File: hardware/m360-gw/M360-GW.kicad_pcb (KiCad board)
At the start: 2 copper layers, 0 parts

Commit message: feat(hardware): posicionamento da M360-GW e LEDs fora da placa (J3)
Placa de 80 × 60 mm, 17 footprints (12 peças, 4 furos M3 e o conector), DRC 0 violações.

Duas restrições comandaram o arranjo, e nenhuma das duas aparece no DRC:

- o mezanino M360-RF ocupa 34,2 × 23 mm **acima** do soquete, mas o courtyard do soquete tem só
  6,2 × 13,8 — confiar nele teria colocado peças embaixo do módulo. J1 fica em x = borda − 27,2
  para o SMA sair pela lateral, e conferi por número que a faixa x 145,8-180 / y 100-123 está
  vazia;
- o D1 mini traz keep-out sobre a antena, na mesma ponta onde fica o USB. Essa ponta encosta na
  borda de cima: a antena não irradia para dentro do cobre e o cabo entra sem abrir a caixa.

Pelo mesmo motivo o H2 não fica no canto — ali cairia sob o mezanino, e a placa teria de ser
parafusada antes de encaixar o módulo. Mesma armadilha já evitada na ACT.

Os LEDs saíram da placa: ficam no painel da caixa e o J3 (JST XH) leva os três pares ao chicote.
São **6 vias em pares ânodo/cátodo**, e não 4 com terra comum, porque o verde é ativo em LOW — o
cátodo dele vai ao D4, não ao GND, de modo que não existe terra comum aos três. Com pares
dedicados os três são ligados da mesma forma no chicote apesar dessa assimetria, e o XH é
chaveado, o que impede inversão no campo. Os resistores de 1 kΩ ficam a bordo: limitação de
corrente não deve viajar no cabo.

O primeiro DRC acusou 5 violações, quatro delas com uma causa só: **girado 90°, o resistor não
fica centrado na origem** — o courtyard vai de y − 11,25 a y + 1,10, quase todo acima do ponto
informado. A fileira subia até 131,75 e entrava no U1, que termina em 134,79. O cálculo ficou
registrado como comentário no place_gw.py, porque se repete na próxima placa. A quinta violação
era o texto de referência do H1 cortado pela borda; como os furos são board-only e ficam fora da
BOM e do arquivo de posição, a serigrafia deles passou a invisível.

Verificação: a troca dos LEDs pelo conector alterou a netlist exatam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
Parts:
- added C1: 10u, Capacitor_THT:CP_Radial_D5.0mm_P2.00mm, F.Cu at (106.0, 140.0)
- added C2: 100n, Capacitor_THT:C_Disc_D5.0mm_W2.5mm_P5.00mm, F.Cu at (115.0, 140.0)
- added C3: 100n, Capacitor_THT:C_Disc_D5.0mm_W2.5mm_P5.00mm, F.Cu at (140.0, 130.0)
- added C4: 100n, Capacitor_THT:C_Disc_D5.0mm_W2.5mm_P5.00mm, F.Cu at (172.0, 140.0)
- added H1: MountingHole_3.2mm_M3, MountingHole_3.2mm_M3, F.Cu at (104.0, 104.0)
- added H2: MountingHole_3.2mm_M3, MountingHole_3.2mm_M3, F.Cu at (176.0, 130.0)
- added H3: MountingHole_3.2mm_M3, MountingHole_3.2mm_M3, F.Cu at (104.0, 156.0)
- added H4: MountingHole_3.2mm_M3, MountingHole_3.2mm_M3, F.Cu at (176.0, 156.0)
- added J1: Mezanino M360-RF, M360:M360-RF_Soquete_2x05, F.Cu at (152.8, 106.4)
- added J2: 5 V ext, M360:TerminalBlock_WJ500V-5.08-2P, F.Cu at (114.0, 152.0)
- added J3: LEDs (painel), Connector_JST:JST_XH_B6B-XH-A_1x06_P2.50mm_Vertical, F.Cu at (130.0, 154.0)
- added R1: 1k, Resistor_THT:R_Axial_DIN0207_L6.3mm_D2.5mm_P10.16mm_Horizontal, F.Cu at (128.0, 148.0)
- added R2: 1k, Resistor_THT:R_Axial_DIN0207_L6.3mm_D2.5mm_P10.16mm_Horizontal, F.Cu at (136.0, 148.0)
- added R3: 1k, Resistor_THT:R_Axial_DIN0207_L6.3mm_D2.5mm_P10.16mm_Horizontal, F.Cu at (144.0, 148.0)
- added R4: 10k, Resistor_THT:R_Axial_DIN0207_L6.3mm_D2.5mm_P10.16mm_Horizontal, F.Cu at (165.0, 140.0)
- added SW1: AP / reset, Button_Switch_THT:SW_PUSH_6mm, F.Cu at (152.0, 152.0)
- added U1: WEMOS D1 mini, RF_Module:WEMOS_D1_mini_light, F.Cu at (110.0, 108.5)
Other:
- board outline added: 80 x 60 mm

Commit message: feat(hardware): roteamento, planos de terra e serigrafia da M360-GW
Roteamento pelo Freerouting 1.9.0 na linha de comando (§11): 0,69 s de roteamento e 4,01 s de
otimização, ~52,77% de melhoria. Resultado: **133 segmentos e 1 via**, zero ligações pendentes
(eram 33). Uma via só não é erro: numa placa 100% THT cada ilha já atravessa as duas faces, e o
roteador troca de camada nos próprios furos.

Planos de GND nas duas faces, isolamento de 0,25 mm, cada um com um polígono contíguo.

O preenchimento acusou `starved_thermal` na ilha 2 do J3 — a ilha de terra do conector dos LEDs,
com 1 raio conectado onde o DRC exige 2. Foi o mesmo sintoma dos RJ45 na LP e na ACT, mas aqui
**o passo 1 da §11.4 bastou**: hastes de 0,35 mm com folga de 0,3 resolveram, sem precisar da
ligação sólida. A geometria explica: as ilhas do JST XH são 1,7 × 1,95 mm a passo de 2,5, o que
deixa só 0,3 mm de corredor horizontal entre ilhas vizinhas — mas os raios verticais passam a
caber assim que a folga cai de 0,5 para 0,3.

Duas armadilhas encontradas e registradas:

- **`set_design_rules` não persiste a largura de trilha que informa.** A ferramenta respondeu
  `trackWidth: 0.25`, mas gravou 0,2 na netclass "Default" do `.kicad_pro` — o valor mínimo — e
  o DSN saiu com `(width 200)`. Quem o roteador lê é o DSN. Corrigido direto no `.kicad_pro` e
  reexportado, agora com `(width 250)`. O aviso está na §11.2. O `kicad-cli` não exporta DSN
  (a lista de subcomandos não tem Specctra), então o MCP é o único caminho automatizado.
- **"Auto-save refused" nem sempre quer dizer o mesmo.** Nas sincronizações o aviso foi
  pessimista duas vezes e a gravação tinha ocorrido; no `add_copper_pour` foi legítimo e a zona
  só existia em memória — conferido no arquivo, onde a única zona era o keep-out do D1 mini.
  Recuperado pelo caminho documentado: recarregar e reaplicar, nunca forçar a gravação.

Serigrafia: marca "Viridiotech.com.br" na faixa livre entre o mezanino e o C3/R4. A primeira
posição encostava na 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
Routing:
- net GND: track 0.00 -> 147.6 mm
- net +3V3: track 0.00 -> 110.9 mm, vias 0 -> 1
- net A0_BTN: track 0.00 -> 108.9 mm
- net LED_YELLOW: track 0.00 -> 57.9 mm
- net MISO: track 0.00 -> 48.7 mm
- net MOSI: track 0.00 -> 48.5 mm
- net NSS: track 0.00 -> 47.5 mm
- net SCK: track 0.00 -> 45.4 mm
- net +5V: track 0.00 -> 41.9 mm
- net LED_GREEN_K: track 0.00 -> 37.5 mm
- net LED_RED: track 0.00 -> 34.1 mm
- net LED_GREEN_A: track 0.00 -> 19.4 mm
- net DIO0: track 0.00 -> 19.3 mm
- net LED_RED_A: track 0.00 -> 18.3 mm
- net LED_YELLOW_A: track 0.00 -> 17.5 mm
- added copper zone on B.Cu, net GND
- added copper zone on F.Cu, net GND
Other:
- board text added: "Viridiotech.com.br"

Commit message: fix(hardware): GW — borne J2 com a entrada dos fios para a borda esquerda
J2 (C8465) a rot 90 em (106; 147): a entrada do fio é o lado -y do footprint
(datasheet, corte A-A) e em rot 0 olhava para dentro da placa. C1 sobe 2 mm.
A placa da GW segue defasada (versão THT) até ser refeita em SMD.

Co-Authored-By: Claude Opus 5 (1M context) <noreply@anthropic.com>
Claude-Session: https://claude.ai/code/session_012t7RkcrXvvpDVjKVimNu18
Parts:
- moved J2 9.43 mm to (106.0, 147.0), turned to 90 degrees
- moved C1 2.00 mm to (106.0, 138.0)
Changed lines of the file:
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@@
 	(footprint "Capacitor_THT:CP_Radial_D5.0mm_P2.00mm"
 		(layer "F.Cu")
-		(at 106 140)
+		(at 106 138)
 		(descr "CP, Radial series, Radial, pin pitch=2.00mm, diameter=5mm, height=7mm, Electrolytic Capacitor")
 		(tags "CP Radial series Radial pin pitch 2.00mm diameter 5mm height 7mm Electrolytic Capacitor")
@@
 	(footprint "M360:TerminalBlock_WJ500V-5.08-2P"
 		(layer "F.Cu")
-		(at 114 152)
+		(at 106 147 90)
 		(descr "WJ500V-5.08-2P")
 		(property "Reference" "J2"
-			(at 0 -4 0)
+			(at 0 -4 90)
 			(layer "F.SilkS")
 			(effects
@@
 		)
 		(property "Value" "5 V ext"
-			(at 0 4 0)
+			(at 0 4 90)
 			(layer "F.Fab")
 			(effects
@@
 		)
 		(property "Datasheet" ""
-			(at 0 0 0)
+			(at 0 0 90)
 			(layer "F.Fab")
 			(hide yes)
@@
 		)
 		(property "Description" ""
-			(at 0 0 0)
+			(at 0 0 90)
 			(layer "F.Fab")
 			(hide yes)
@@
 		)
 		(property "LCSC Part" "C8465"
-			(at 0 0 0)
+			(at 0 0 90)
 			(layer "F.Fab")
 			(hide yes)
@@
 		(duplicate_pad_numbers_are_jumpers no)
 		(fp_line
+			(start 5.08 -5.64)
+			(end -5.05 -5.64)
+			(stroke
+				(width 0.25)
+				(type solid)
+			)
+			(layer "F.SilkS")
+		)
+		(fp_line
 			(start -5.68 -4.75)
 			(end -5.68 -3.75)
@@
 		)
 		(fp_line
+			(start -5.08 -4.5)
+			(end -5.68 -4.75)
+			(stroke
+				(width 0.25)
+				(type solid)
+			)
+			(layer "F.SilkS")
+		)
+		(fp_line
 			(start -5.68 -3.75)
 			(end -5.08 -4)
@@
 		)
 		(fp_line
+			(start -5.08 3)
+			(end -5.68 2.75)
+			(stroke
+				(width 0.25)
+				(type solid)
+			)
+			(layer "F.SilkS")
+		)
+		(fp_line
 			(start -5.68 3.75)
 			(end -5.08 3.5)
@@
 		)
 		(fp_line
-			(start -5.08 -4.5)
-			(end -5.68 -4.75)
+			(start 5.08 4.52)
+			(end 5.08 -5.64)
 			(stroke
 				(width 0.25)
@@
 		)
 		(fp_line
-			(start -5.08 3)
-			(end -5.68 2.75)
+			(start 5.08 4.52)
+			(end -5.05 4.52)
 			(stroke
 				(width 0.25)
@@
 			(start -5.08 4.52)
 			(end -5.08 -5.64)
-			(stroke
-				(width 0.25)
-				(type solid)
-			)
-			(layer "F.SilkS")
-		)
-		(fp_line
-			(start 5.08 -5.64)
-			(end -5.05 -5.64)
-			(stroke
-				(width 0.25)
-				(type solid)
-			)
-			(layer "F.SilkS")
-		)
-		(fp_line
-			(start 5.08 4.52)
-			(end -5.05 4.52)
-			(stroke
-				(width 0.25)
-				(type solid)
-			)
-			(layer "F.SilkS")
-		)
-		(fp_line
-			(start 5.08 4.52)
-			(end 5.08 -5.64)
 			(stroke
 				(width 0.25)
@@
 			)
 			(fill no)
+			(layer "F.SilkS")
+		)
+		(fp_poly
+			(pts
+				(xy 2.080006 -5.499989) (xy 3.080004 -5.499989) (xy 3.080004 -3.499993) (xy 3.580003 -3.499993)
+				(xy 2.580005 -2.499995) (xy 1.580007 -3.499993) (xy 2.080006 -3.499993) (xy 2.080006 -5.499989)
+			)
+			(stroke
+				(width 0)
+				(type solid)
+			)
+			(fill yes)
 			(layer "F.SilkS")
 		)
@@
 			(layer "F.SilkS")
 		)
-		(fp_poly
-			(pts
-				(xy 2.080006 -5.499989) (xy 3.080004 -5.499989) (xy 3.080004 -3.499993) (xy 3.580003 -3.499993)
-				(xy 2.580005 -2.499995) (xy 1.580007 -3.499993) (xy 2.080006 -3.499993) (xy 2.080006 -5.499989)
-			)
-			(stroke
-				(width 0)
-				(type solid)
-			)
-			(fill yes)
-			(layer "F.SilkS")
+		(fp_line
+			(start 5.21 -5.5)
+			(end 5.21 4.5)
+			(stroke
+				(width 0.05)
+				(type solid)
+			)
+			(layer "F.CrtYd")
 		)
 		(fp_line
@@
 		)
 		(fp_line
+			(start 5.21 4.5)
+			(end -5.21 4.5)
+			(stroke
+				(width 0.05)
+				(type solid)
+			)
+			(layer "F.CrtYd")
+		)
+		(fp_line
 			(start -5.21 4.5)
 			(end -5.21 -5.5)
@@
 			(layer "F.CrtYd")
 		)
-		(fp_line
-			(start 5.21 -5.5)
-			(end 5.21 4.5)
-			(stroke
-				(width 0.05)
-				(type solid)
-			)
-			(layer "F.CrtYd")
-		)
-		(fp_line
-			(start 5.21 4.5)
-			(end -5.21 4.5)
-			(stroke
-				(width 0.05)
-				(type solid)
-			)
-			(layer "F.CrtYd")
+		(fp_circle
+			(center 2.54 0)
+			(end 2.82 0)
+			(stroke
+				(width 0.55)
+				(type solid)
+			)
+			(fill no)
+			(layer "F.Fab")
 		)
 		(fp_circle
@@
 			(layer "F.Fab")
 		)
-		(fp_circle
-			(center 2.54 0)
-			(end 2.82 0)
-			(stroke
-				(width 0.55)
-				(type solid)
-			)
-			(fill no)
-			(layer "F.Fab")
-		)
 		(fp_text user "${REFERENCE}"
-			(at 0 0 0)
+			(at 0 0 90)
 			(layer "F.Fab")
 			(effects
@@
 		)
 		(pad "1" thru_hole circle
-			(at -2.54 0 180)
+			(at -2.54 0 270)
 			(size 2 2)
 			(drill 1.300022)
@@
 		)
 		(pad "2" thru_hole circle
-			(at 2.54 0 180)
+			(at 2.54 0 270)
 			(size 2 2)
 			(drill 1.300022)

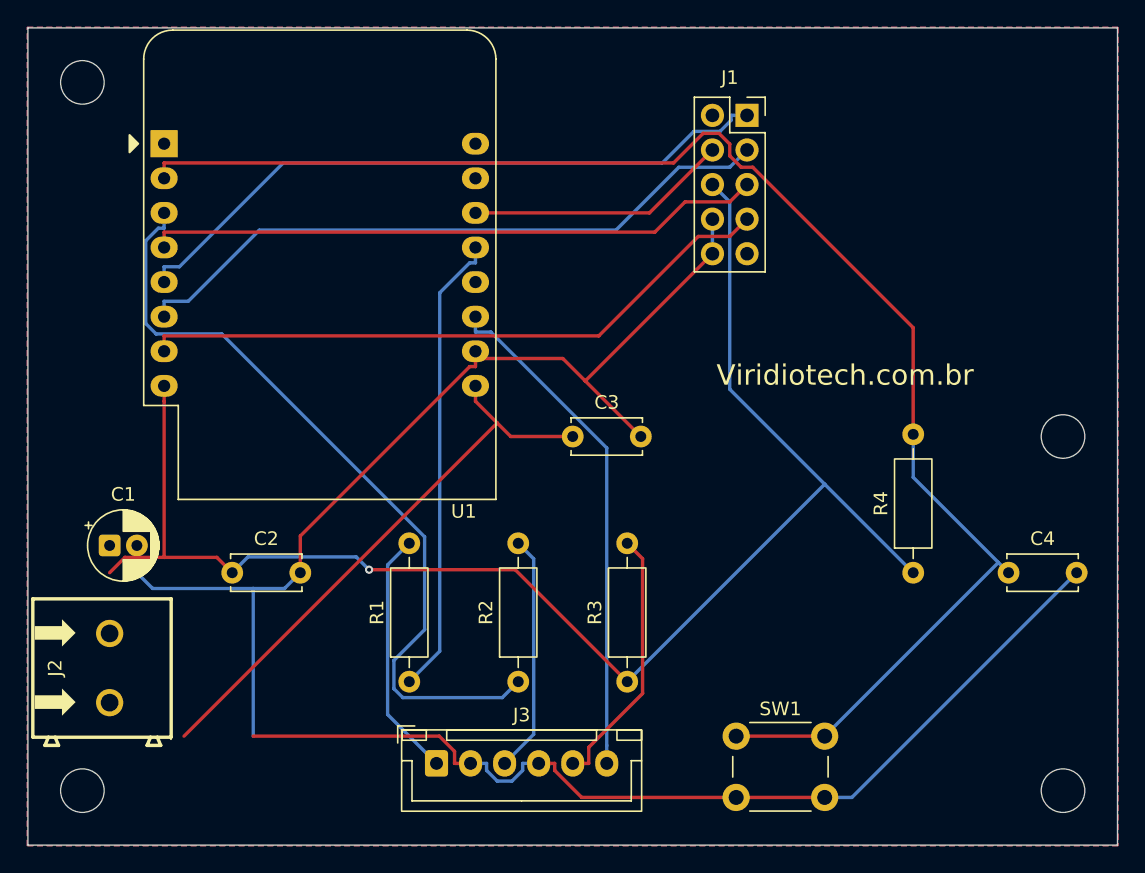
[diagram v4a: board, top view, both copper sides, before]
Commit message: feat(hardware): placa da M360-GW refeita em SMD e arquivos de fabricação
- 10 footprints THT apagados, 15 SMD sincronizados do esquemático
- place_gw.py reescrito: D1 mini com a antena na borda de cima, mezanino com
  o SMA na borda direita, borne J2 a rot 90 (entrada dos fios na borda),
  reed a 1 mm da borda esquerda junto do A0, cadeia SS14 -> PTC -> SMAJ,
  resistores dos LEDs e 2N7002 junto do J3, fiduciais
- classe Power em VIN_RAW, VIN_POL, +5V e +3V3
- vias_gnd.py: isolamento da classe do pad e áreas proibidas de footprint
  (keep-out da antena do D1 mini)
- fabricacao/: 14 peças, todas com LCSC

DRC --severity-all 0/0, paridade idêntica.

Co-Authored-By: Claude Opus 5 (1M context) <noreply@anthropic.com>
Claude-Session: https://claude.ai/code/session_012t7RkcrXvvpDVjKVimNu18
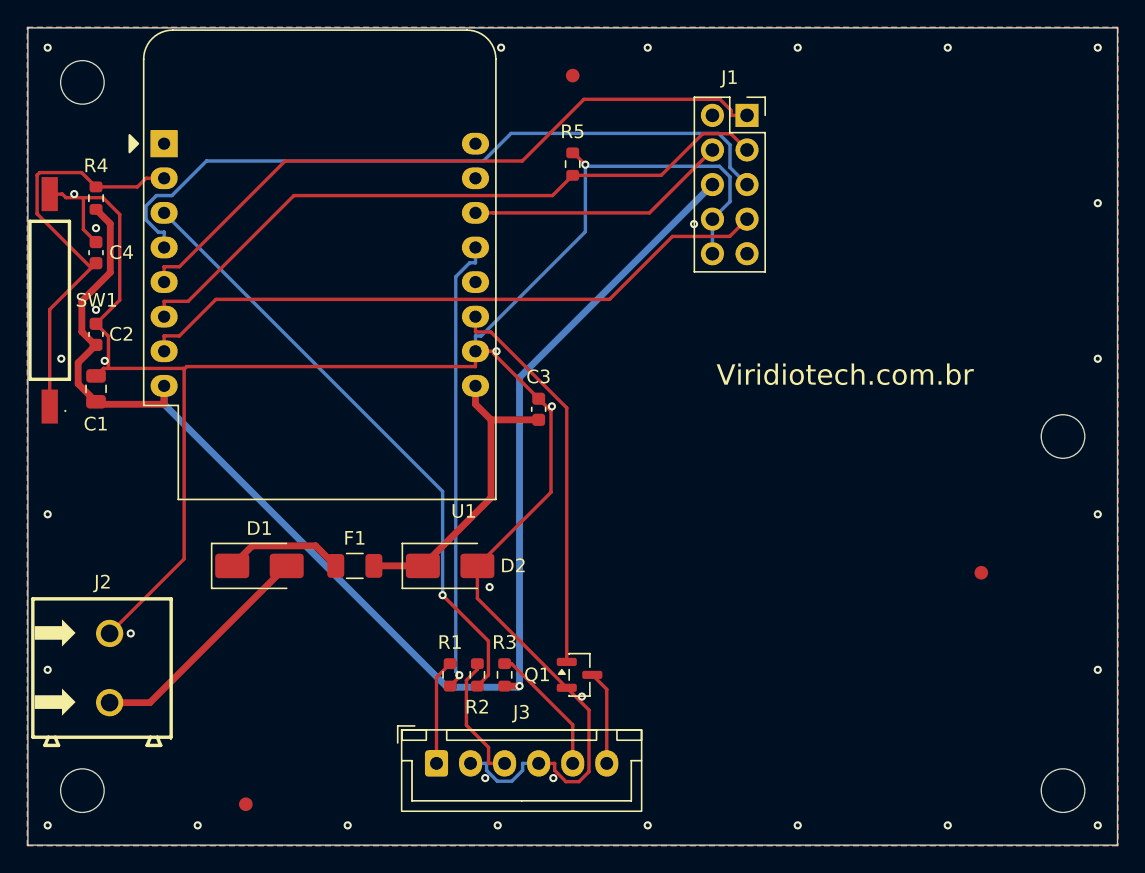
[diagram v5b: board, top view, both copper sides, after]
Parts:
- added D1: SS14, Diode_SMD:D_SMA, F.Cu at (117.0, 139.5)
- added D2: SMAJ5.0A, Diode_SMD:D_SMA, F.Cu at (131.0, 139.5)
- added F1: 500mA, Fuse:Fuse_1206_3216Metric, F.Cu at (124.0, 139.5)
- added FID1: Fiducial_1mm_Mask2mm, Fiducial_1mm_Mask2mm, F.Cu at (140.0, 103.5)
- added FID2: Fiducial_1mm_Mask2mm, Fiducial_1mm_Mask2mm, F.Cu at (170.0, 140.0)
- added FID3: Fiducial_1mm_Mask2mm, Fiducial_1mm_Mask2mm, F.Cu at (116.0, 157.0)
- added Q1: 2N7002, Package_TO_SOT_SMD:SOT-23, F.Cu at (140.5, 147.5)
- added R5: 100k, Resistor_SMD:R_0603_1608Metric, F.Cu at (140.0, 110.0)
- C1: value 10u -> 10uF; footprint Capacitor_THT:CP_Radial_D5.0mm_P2.00mm -> Capacitor_SMD:C_0805_2012Metric
- C2, C3, C4: value 100n -> 100nF; footprint Capacitor_THT:C_Disc_D5.0mm_W2.5mm_P5.00mm -> Capacitor_SMD:C_0603_1608Metric
- R1, R2, R3: value 1k -> 470; footprint Resistor_THT:R_Axial_DIN0207_L6.3mm_D2.5mm_P10.16mm_Horizontal -> Resistor_SMD:R_0603_1608Metric
- R4: footprint Resistor_THT:R_Axial_DIN0207_L6.3mm_D2.5mm_P10.16mm_Horizontal -> Resistor_SMD:R_0603_1608Metric
- SW1: value AP / reset -> Reed; footprint Button_Switch_THT:SW_PUSH_6mm -> M360:Reed_Littelfuse_59170
- moved C4 71.0 mm to (105.0, 116.5), turned to 90 degrees
- moved R4 66.0 mm to (105.0, 112.5)
- moved SW1 59.7 mm to (101.6, 120.0), turned to 90 degrees
- moved C2 20.2 mm to (105.0, 122.5), turned to 90 degrees
- moved C1 11.5 mm to (105.0, 126.5), turned to 90 degrees
- moved R3 9.01 mm to (135.0, 147.5)
- moved C3 3.20 mm to (137.5, 128.0), turned to 90 degrees
- moved R1 3.04 mm to (131.0, 147.5)
- moved R2 3.04 mm to (133.0, 147.5)
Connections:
- J2 pad 1: +5V -> VIN_RAW
- U1 pad 11: LED_GREEN_K -> LED_GREEN
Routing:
- net A0_BTN: track 108.9 -> 30.5 mm
- net LED_GREEN_K: track 37.5 -> 6.94 mm
- net LED_GREEN: track 0.00 -> 28.8 mm
- net +5V: track 41.9 -> 22.9 mm
- net VIN_RAW: track 0.00 -> 17.2 mm
- net LED_YELLOW: track 57.9 -> 44.9 mm, vias 0 -> 1
- net GND: track 147.6 -> 159.6 mm, vias 0 -> 34
- net LED_RED_A: track 18.3 -> 7.74 mm
- net LED_GREEN_A: track 19.4 -> 9.69 mm
- net VIN_POL: track 0.00 -> 8.82 mm
- net LED_YELLOW_A: track 17.5 -> 9.51 mm
- net +3V3: track 110.9 -> 103.3 mm
- net SCK: track 45.4 -> 52.7 mm
- net MOSI: track 48.5 -> 49.5 mm
- net MISO: track 48.7 -> 49.7 mm
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
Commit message: fix(hardware): GW — D1 mini a 180° com o USB na borda de cima
- U1 girado: USB na borda de cima (cabo entra sem abrir a caixa), antena do
  ESP para dentro da placa, com o keep-out do footprint preservado
- colunas de pinos trocadas de lado: C1, C2, R4, C4 e R5 entre o módulo e o
  mezanino; C3 junto do pino de 5 V
- reed SW1 na borda direita, entre o H2 e o H4 (borda do SMA, rente à parede)
- LED_RED desenhado à mão em B.Cu (o Freerouting não passava pela zona da
  antena); via do LED_YELLOW afastada do pad de +3V3
- fabricacao/ regenerado (14 peças)

DRC --severity-all 0/0, paridade idêntica.

Co-Authored-By: Claude Opus 5 <noreply@anthropic.com>
Claude-Session: https://claude.ai/code/session_012t7RkcrXvvpDVjKVimNu18
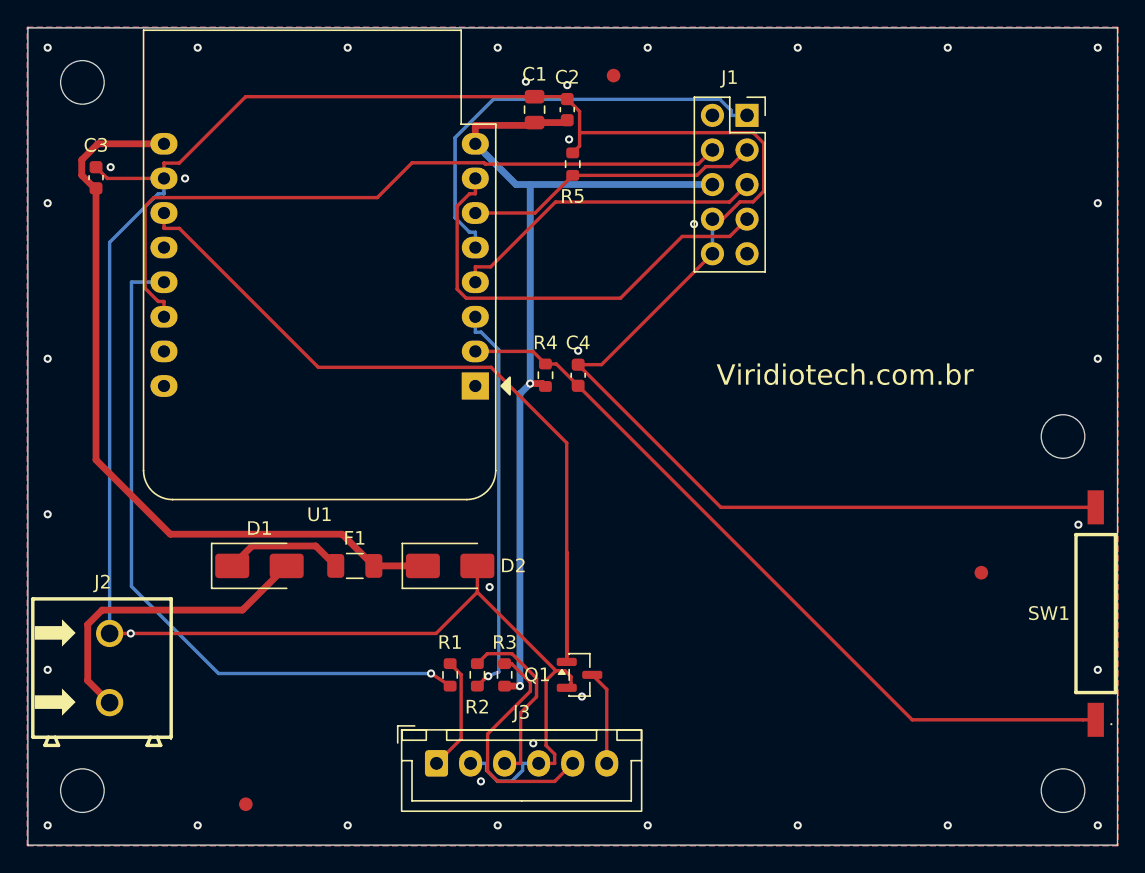
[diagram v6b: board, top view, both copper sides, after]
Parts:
- moved SW1 80.2 mm to (178.4, 143.0)
- moved C2 38.3 mm to (139.6, 106.0)
- moved C1 38.2 mm to (137.2, 106.0)
- moved C3 36.7 mm to (105.0, 111.0)
- moved C4 36.5 mm to (140.4, 125.5)
- moved R4 35.5 mm to (138.0, 125.5)
- moved U1 29.0 mm to (132.8, 126.3), turned to 180 degrees
- moved FID1 3.00 mm to (143.0, 103.5)
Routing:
- net GND: track 159.6 -> 213.9 mm, vias 34 -> 36
- net +3V3: track 103.3 -> 66.4 mm, vias 1 -> 2
- net +5V: track 22.9 -> 56.3 mm
- net DIO0: track 19.3 -> 52.4 mm
- net LED_GREEN: track 28.8 -> 61.3 mm
- net SCK: track 52.7 -> 23.6 mm
- net MOSI: track 49.5 -> 21.9 mm
- net A0_BTN: track 30.5 -> 56.8 mm
- net LED_RED: track 33.4 -> 51.1 mm
- net MISO: track 49.7 -> 32.2 mm
- net LED_YELLOW: track 44.9 -> 29.0 mm
- net NSS: track 47.5 -> 32.9 mm
- net LED_GREEN_A: track 9.69 -> 17.4 mm
- net VIN_RAW: track 17.2 -> 22.8 mm
- net LED_YELLOW_A: track 9.51 -> 13.3 mm
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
